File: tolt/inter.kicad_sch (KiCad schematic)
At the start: 12 parts, among them U2 L6491, U3 L6491, U4 L6491

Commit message: modified:   tolt/inter.kicad_sch 	modified:   tolt/stm32.kicad_sch
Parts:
- added C16, C18, C20: 100n, Capacitor_SMD:C_0402_1005Metric, symbol Device:C
- added D1, D2, D3: STTH2R06A, Diode_SMD:D_SMA, symbol Diode:STTH212S
- added R1, R2, R3: R, symbol Device:R
- renumbered C21 to C15, C22 to C17, C23 to C19, C15 to C21, C16 to C22, C17 to C23, C18 to C24, C19 to C25, C20 to C26, U4 to U3, U3 to U4
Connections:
- net +12V: now also D1.2 (A), D2.2 (A), D3.2 (A)
- net GND: now also C16.1, C18.1, C20.1, R1.2, R2.2, R3.2
- net L_A: now reaches U2.1 (~{LIN})
- net Ph_a: now reaches U2.12 (OUT)
- net G_H_A: now reaches U2.13 (HVG)
- net at C15.1, U2.14 (BOOT): now also D1.1 (K)
- net BRK: now reaches U2.2 (~{SD}/OD)
- net BRK: now also U3.2 (~{SD}/OD), U4.2 (~{SD}/OD)
- net H_A: now reaches U2.3 (HIN)
- net at U2.5 (DT): now also C16.2, R1.1
- net G_L_A: now reaches U2.8 (LVG)
- net L_B: now reaches U4.1 (~{LIN})
- net L_B: now also U3.1 (~{LIN})
- net Ph_c: now reaches U4.12 (OUT)
- net G_H_C: now reaches U4.13 (HVG)
- net at C19.1, U4.14 (BOOT): now also D3.1 (K)
- net H_B: now reaches U4.3 (HIN)
- net H_B: now also U3.3 (HIN)
- net at U4.5 (DT): now also C20.2, R3.1
- net G_L_C: now reaches U4.8 (LVG)
- net Ph_b: now reaches U3.12 (OUT)
- net G_H_B: now reaches U3.13 (HVG)
- net at C17.1, U3.14 (BOOT): now also D2.1 (K)
- net at U3.5 (DT): now also C18.2, R2.1
- net G_L_B: now reaches U3.8 (LVG)
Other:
- note added: "external bootstrap optionnal for test Place only footprint"

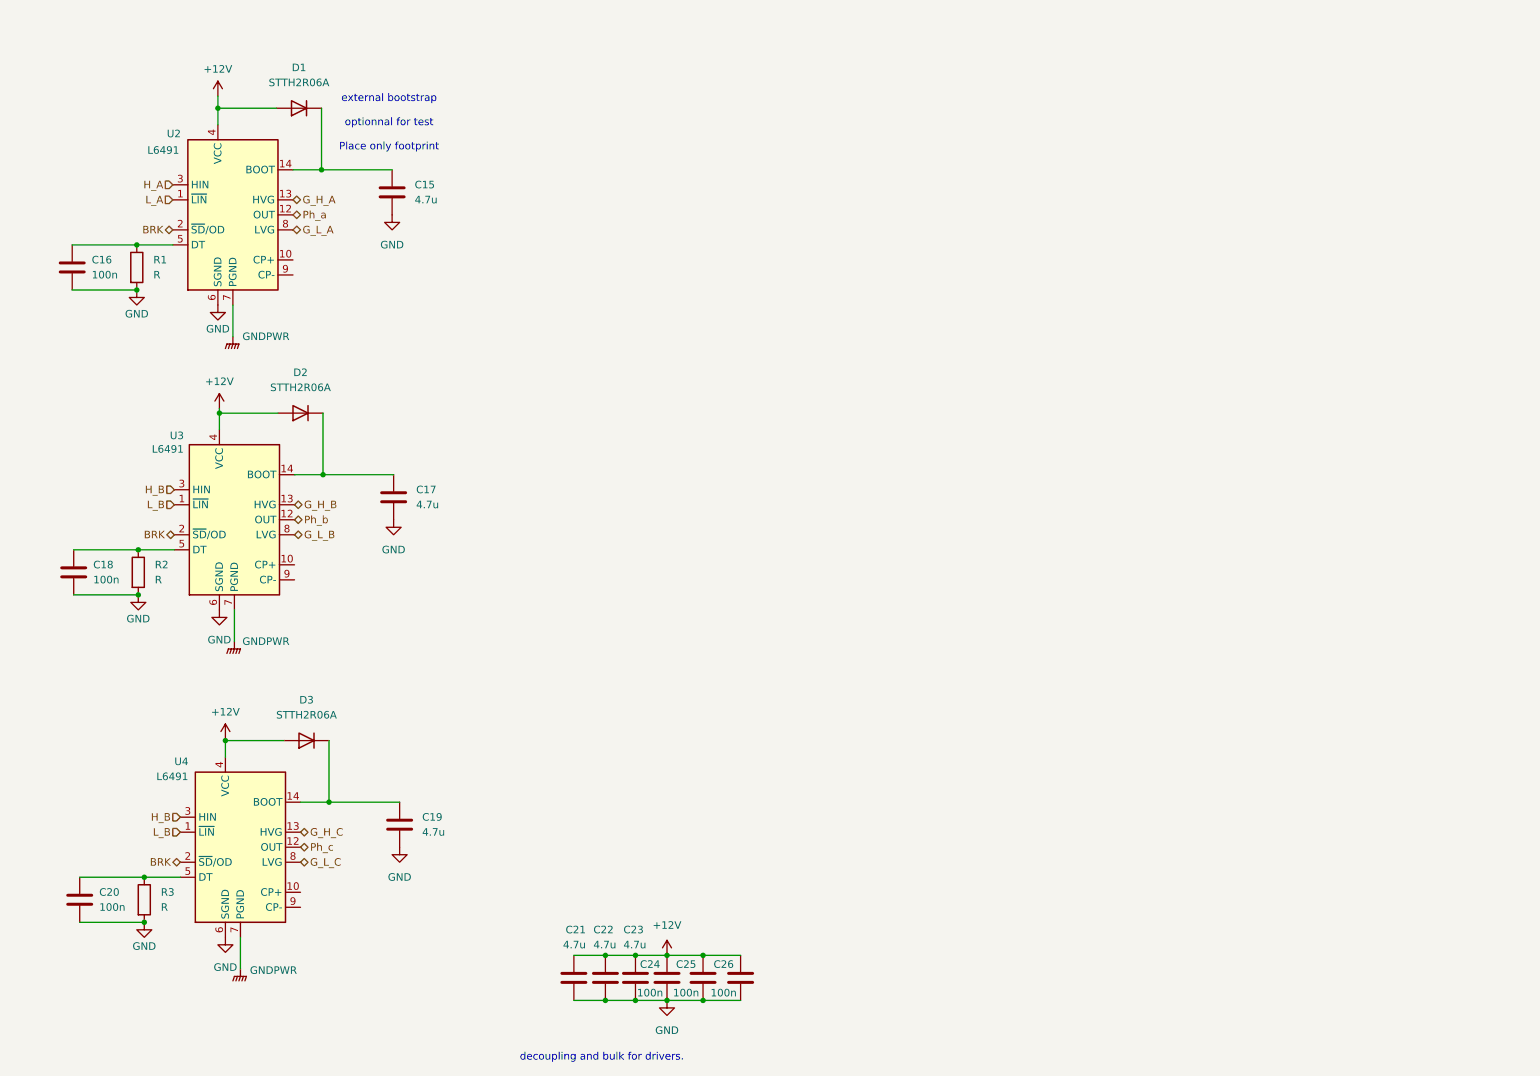
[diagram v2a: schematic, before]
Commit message: modified:   tolt/inter.kicad_sch 	modified:   tolt/powerstage.kicad_sch
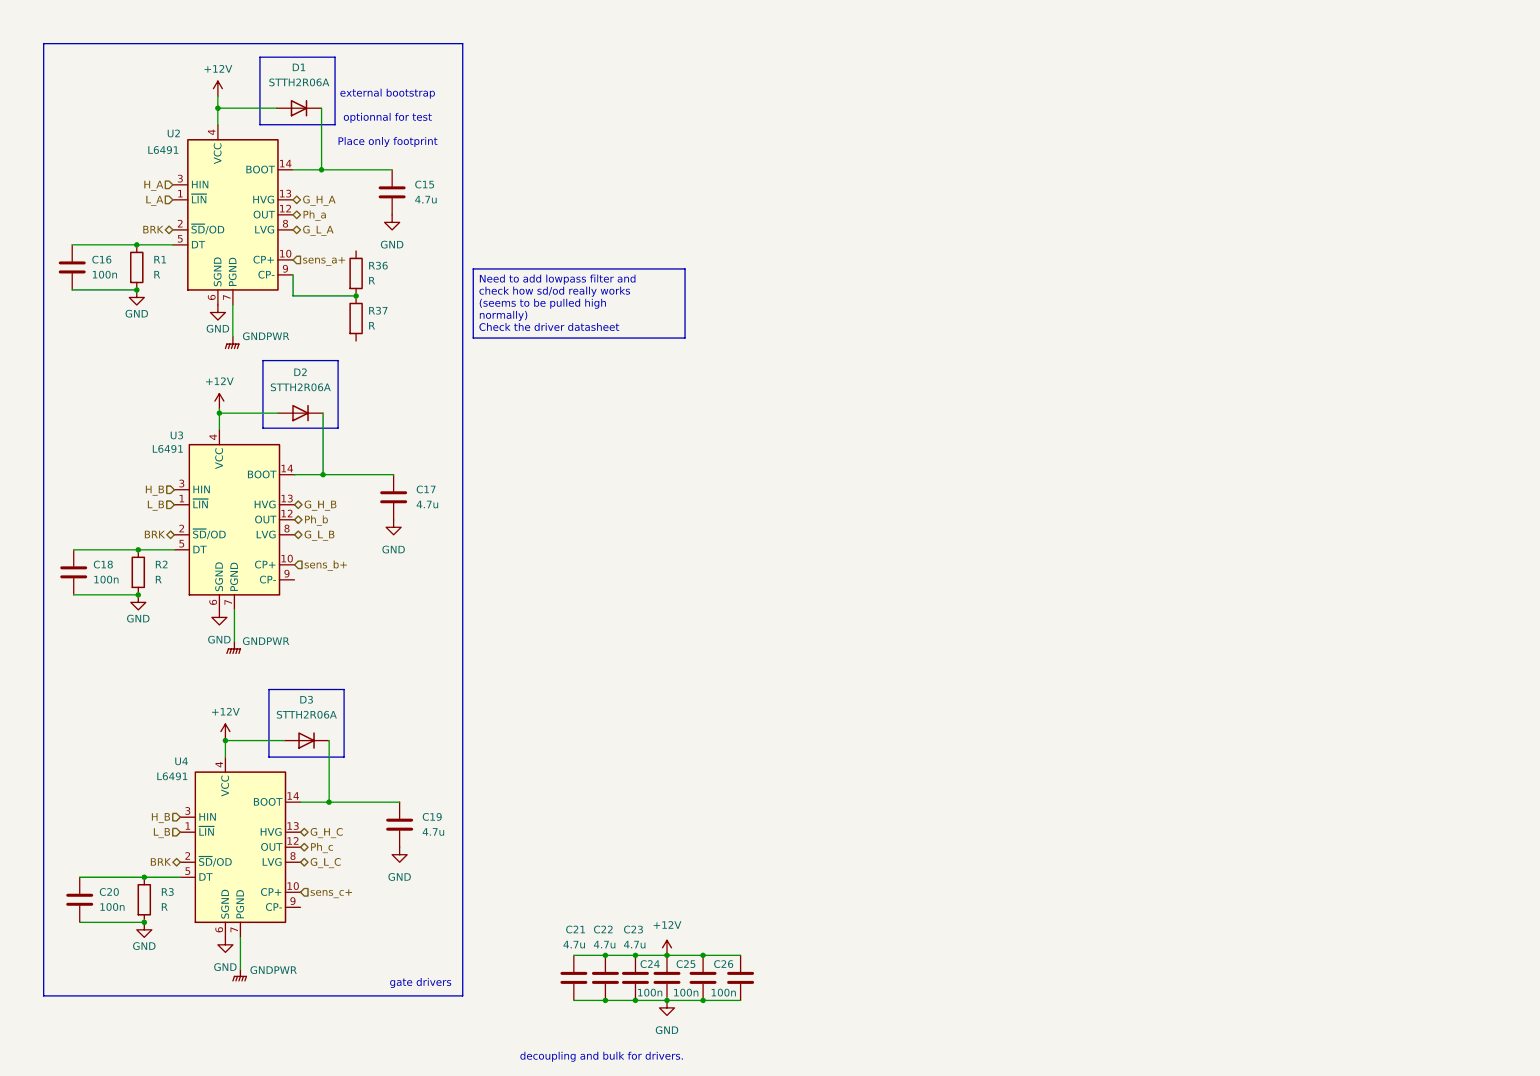
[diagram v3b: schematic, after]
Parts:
- added R36, R37: R, symbol Device:R
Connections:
- net sens_a+: now reaches U2.10 (CP+)
- net at U2.9 (CP-): now also R36.2, R37.1
- net sens_c+: now reaches U4.10 (CP+)
- net sens_b+: now reaches U3.10 (CP+)
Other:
- note added: "gate drivers"

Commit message: i hate RC Filters
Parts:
- C16, C18, C20: value 100n -> 220nF
- R1, R2, R3: value R -> 0
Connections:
- net sens_a+ renamed SENS_A+
- net sens_b+ renamed SENS_B+
- net sens_c+ renamed SENS_C+

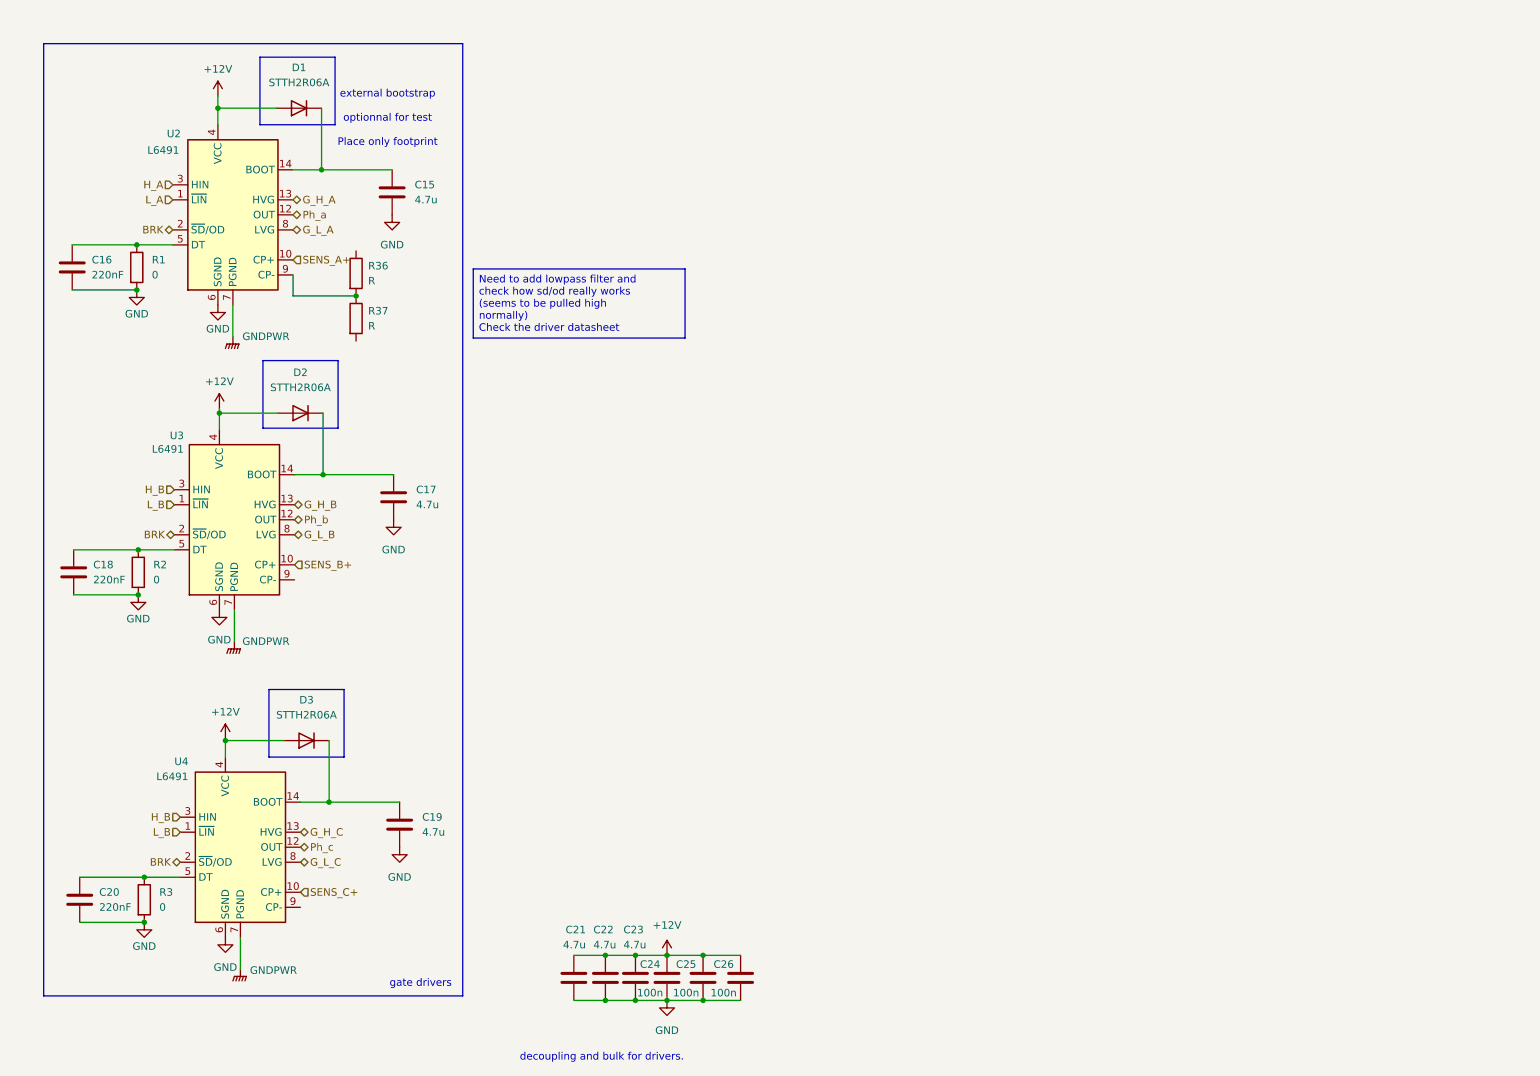
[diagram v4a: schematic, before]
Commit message: modified:   tolt/inter.kicad_sch 	modified:   tolt/stm32.kicad_sch 	modified:   tolt/tolt.kicad_sch
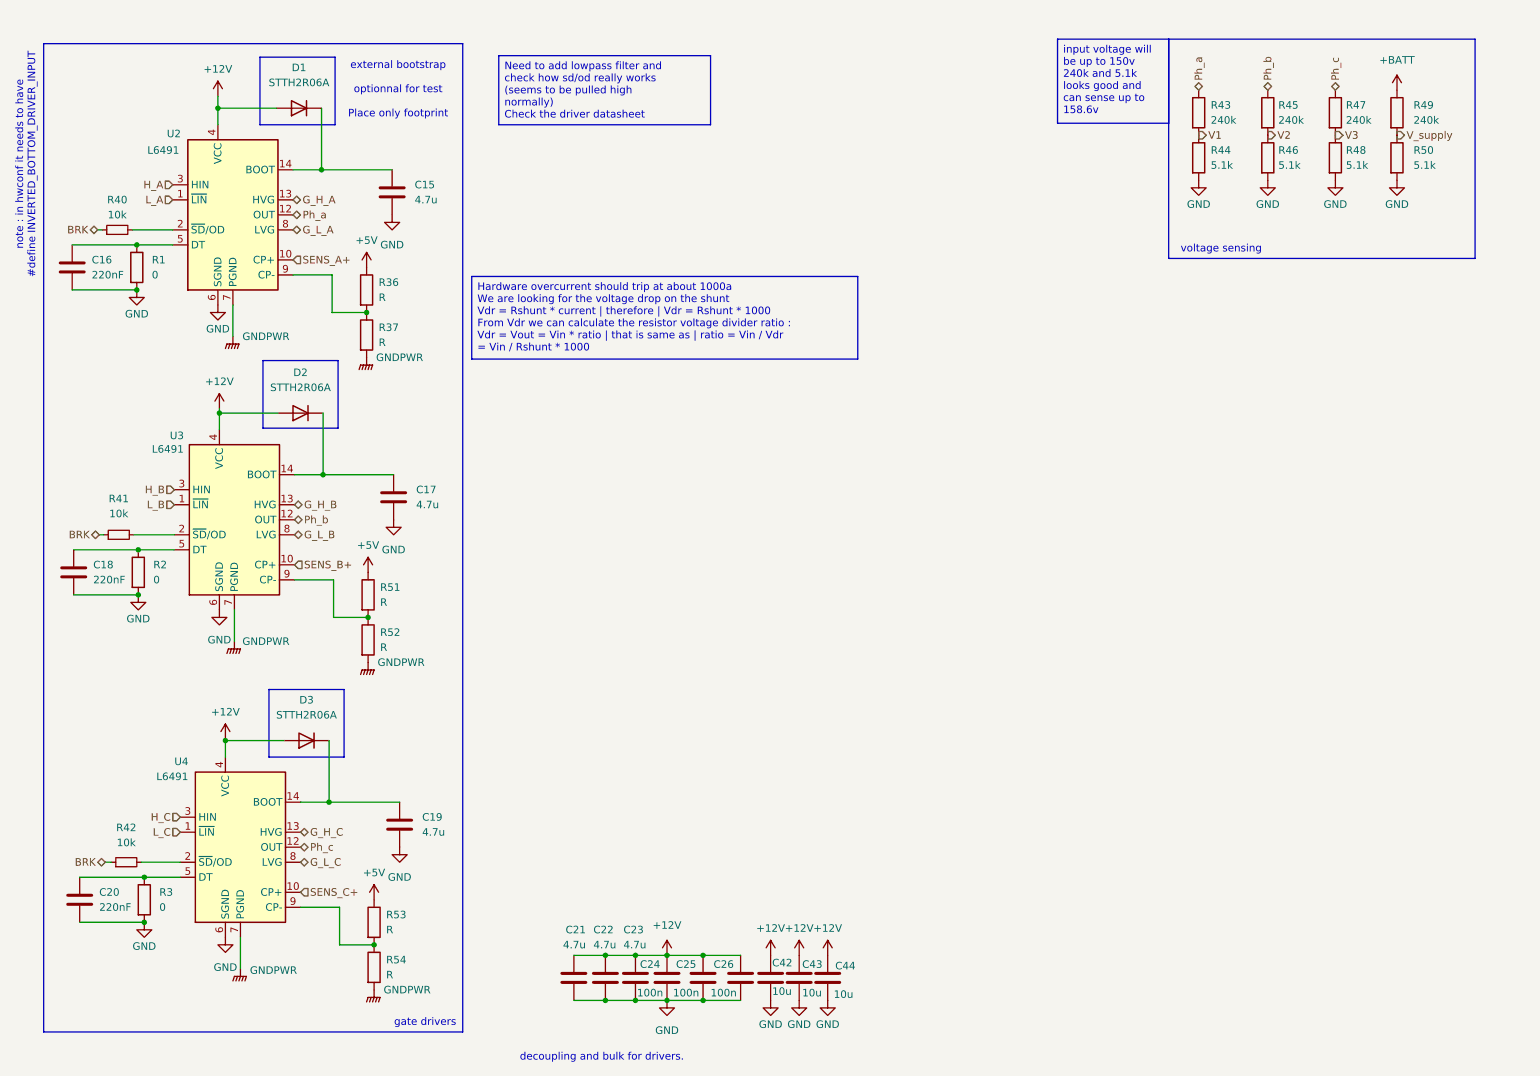
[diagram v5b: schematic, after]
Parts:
- added C42, C43, C44: 10u, symbol Device:C
- added R40, R41, R42: 10k, Resistor_SMD:R_0603_1608Metric, symbol Device:R_Small
- added R43, R45, R47, R49: 240k, symbol Device:R
- added R44, R46, R48, R50: 5.1k, symbol Device:R
- added R51, R52, R53, R54: R, symbol Device:R
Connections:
- net +12V: now also C42.1, C43.1, C44.1
- net BRK: now also R40.1, R41.1, R42.1; no longer U2.2 (~{SD}/OD), U3.2 (~{SD}/OD), U4.2 (~{SD}/OD)
- net GND: now also C42.2, C43.2, C44.2, R44.2, R46.2, R48.2, R50.2
- net GNDPWR: now also R37.2, R52.2, R54.2
- net H_B: no longer U4.3 (HIN)
- net L_B: no longer U4.1 (~{LIN})
- net Ph_a: now also R43.1
- net Ph_b: now also R45.1
- net Ph_c: now also R47.1
- net +5V: now reaches R36.1
- net +5V: now also R51.1, R53.1
- net at U4.9 (CP-): now also R53.2, R54.1
- net at U3.9 (CP-): now also R51.2, R52.1
- new net: R40.2, U2.2 (~{SD}/OD)
- new net: R41.2, U3.2 (~{SD}/OD)
- new net: R42.2, U4.2 (~{SD}/OD)
- new net +BATT: R49.1
- new net H_C: U4.3 (HIN)
- new net L_C: U4.1 (~{LIN})
- new net V1: R43.2, R44.1
- new net V2: R45.2, R46.1
- new net V3: R47.2, R48.1
- new net V_supply: R49.2, R50.1
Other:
- note added: "note : in hwconf it needs to have #define INVERTED_BOTTOM_DRIVER_INPUT"
- note added: "voltage sensing"
- moved on the sheet: R36, R37

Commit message: modified:   tolt/inter.kicad_sch 	modified:   tolt/powerstage.kicad_sch 	modified:   tolt/stm32.kicad_sch 	modified:   tolt/tolt.kicad_sch
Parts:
- added C51, C52, C53: 4.7u, Capacitor_SMD:C_0603_1608Metric_Pad1.08x0.95mm_HandSolder, symbol Device:C
- added C54, C56, C57: 100n, Capacitor_SMD:C_0603_1608Metric_Pad1.08x0.95mm_HandSolder, symbol Device:C_Small
- added C55: 100n, symbol Device:C_Small
- added R55, R56, R57: 10k, Resistor_SMD:R_0603_1608Metric, symbol Device:R_Small
- R1, R2, R3: now not fitted
- R36, R51, R53: value R -> 320k
- R37, R52, R54: value R -> 10k
- R49: value 240k -> 480k
- R50: value 5.1k -> 10.2k
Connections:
- net BRK: now also R40.2; no longer R40.1
- net GND: now also C54.2, C55.2, C56.2, C57.2
- net GNDPWR: now also C51.2, C52.2, C53.2
- net V1: now also C54.1
- net V2: now also C55.1
- net V3: now also C57.1
- net V_supply: now also C56.1
- net at U2.2 (~{SD}/OD): now also R40.1, R55.2; no longer R40.2
- net at R36.2, R37.1, U2.9 (CP-): now also C51.1
- net at R41.2, U3.2 (~{SD}/OD): now also R56.2
- net at R53.2, R54.1, U4.9 (CP-): now also C53.1
- net at R51.2, R52.1, U3.9 (CP-): now also C52.1
- net at R42.2, U4.2 (~{SD}/OD): now also R57.2
- net +5V renamed +3V3
- net +3V3: now also R55.1, R56.1, R57.1
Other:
- moved on the sheet: R40, R41, R42, R43, R44, R45, R46, R47, R48, R49, R50

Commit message: Converters
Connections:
- net +3V3 renamed VCC

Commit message: Reapply "Merge branch 'main' of https://github.com/LJBoxx/bigtolt"
This reverts commit 10d1035653869a11abcc4dc45a35a471baa73785.
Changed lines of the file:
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@@
 	(text "note : in hwconf it needs to have \n#define INVERTED_BOTTOM_DRIVER_INPUT"
 		(exclude_from_sim no)
-		(at 24.384 40.64 90)
+		(at 47.244 17.272 0)
 		(effects
 			(font
@@
 	(text_box "Need to add lowpass filter and check how sd/od really works (seems to be pulled high normally)\nCheck the driver datasheet\n"
 		(exclude_from_sim no)
-		(at 104.394 22.098 0)
+		(at 98.298 20.066 0)
 		(size 35.814 11.684)
 		(margins 0.9525 0.9525 0.9525 0.9525)
@@
 	(text_box "Hardware overcurrent should trip at about 1000a\nWe are looking for the voltage drop on the shunt\nVdr = Rshunt * current | therefore | Vdr = Rshunt * 1000\nFrom Vdr we can calculate the resistor voltage divider ratio : \nVdr = Vout = Vin * ratio | that is same as | ratio = Vin / Vdr = Vin / Rshunt * 1000 \nHere ratio of 0.1/3.3 therefore 320k and 10k \nchange 320k to 980k for 0.1mr\n"
 		(exclude_from_sim no)
-		(at 99.822 59.436 0)
+		(at 98.298 59.436 0)
 		(size 65.278 17.78)
 		(margins 0.9525 0.9525 0.9525 0.9525)
